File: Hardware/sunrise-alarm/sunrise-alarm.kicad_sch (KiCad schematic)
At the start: 35 parts, among them J1 Conn_01x08_Male

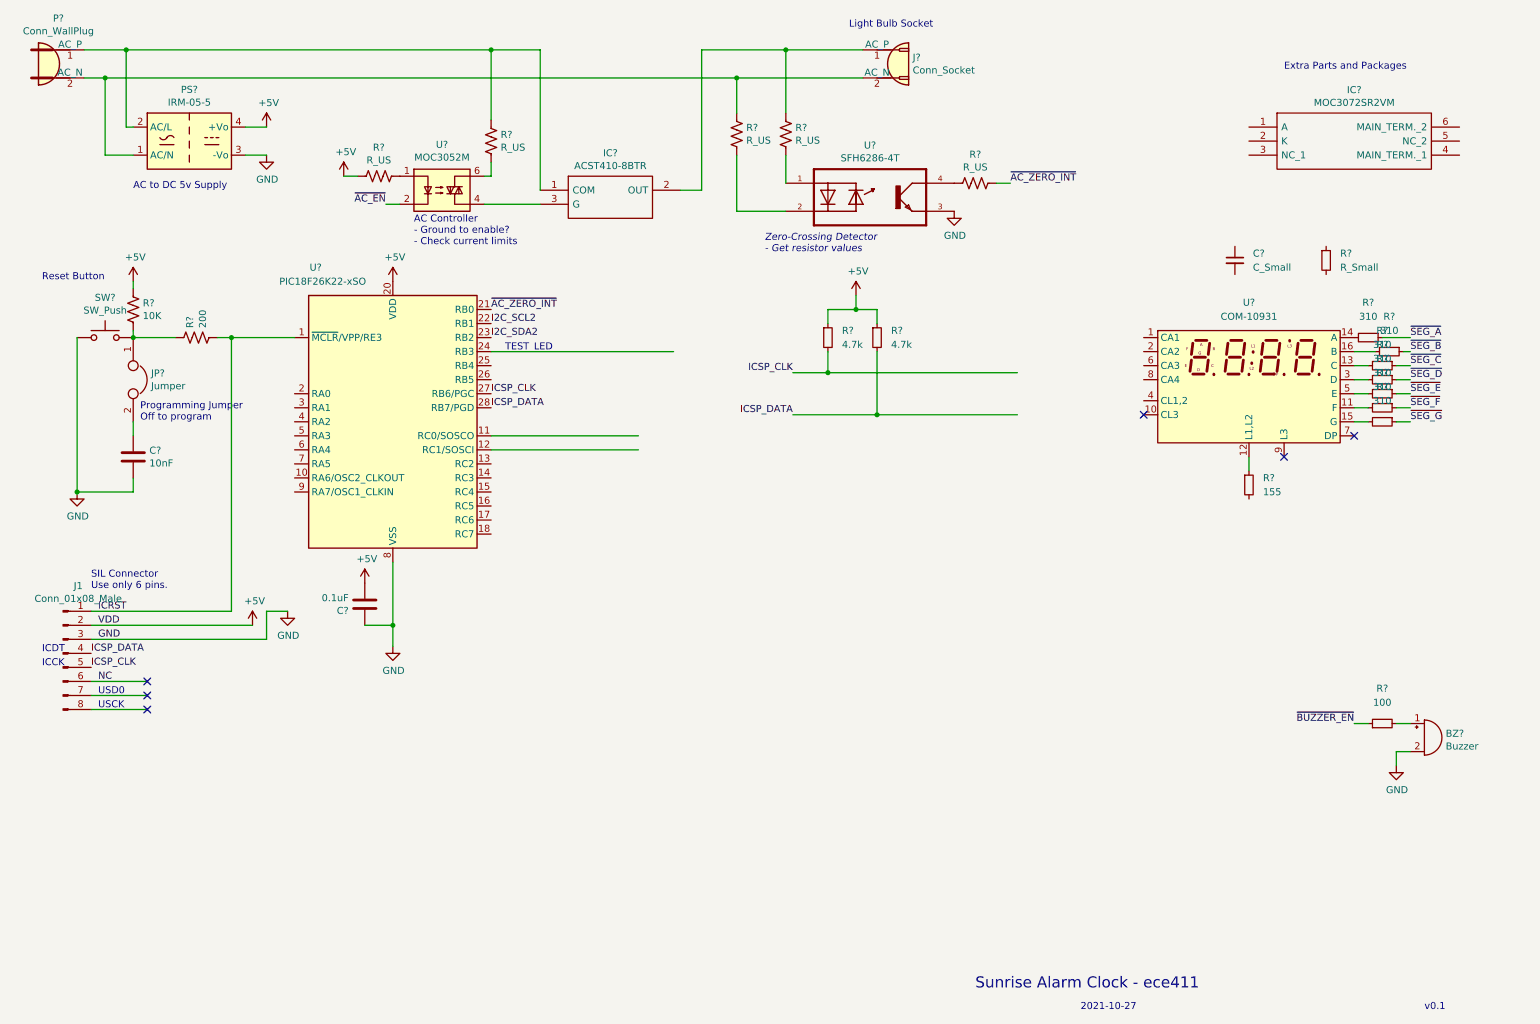
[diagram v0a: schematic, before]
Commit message: Schematic Updates
Changed to 3.3v supply to accommodate gesture sensor.
Added gesture sensor.
Added test led.
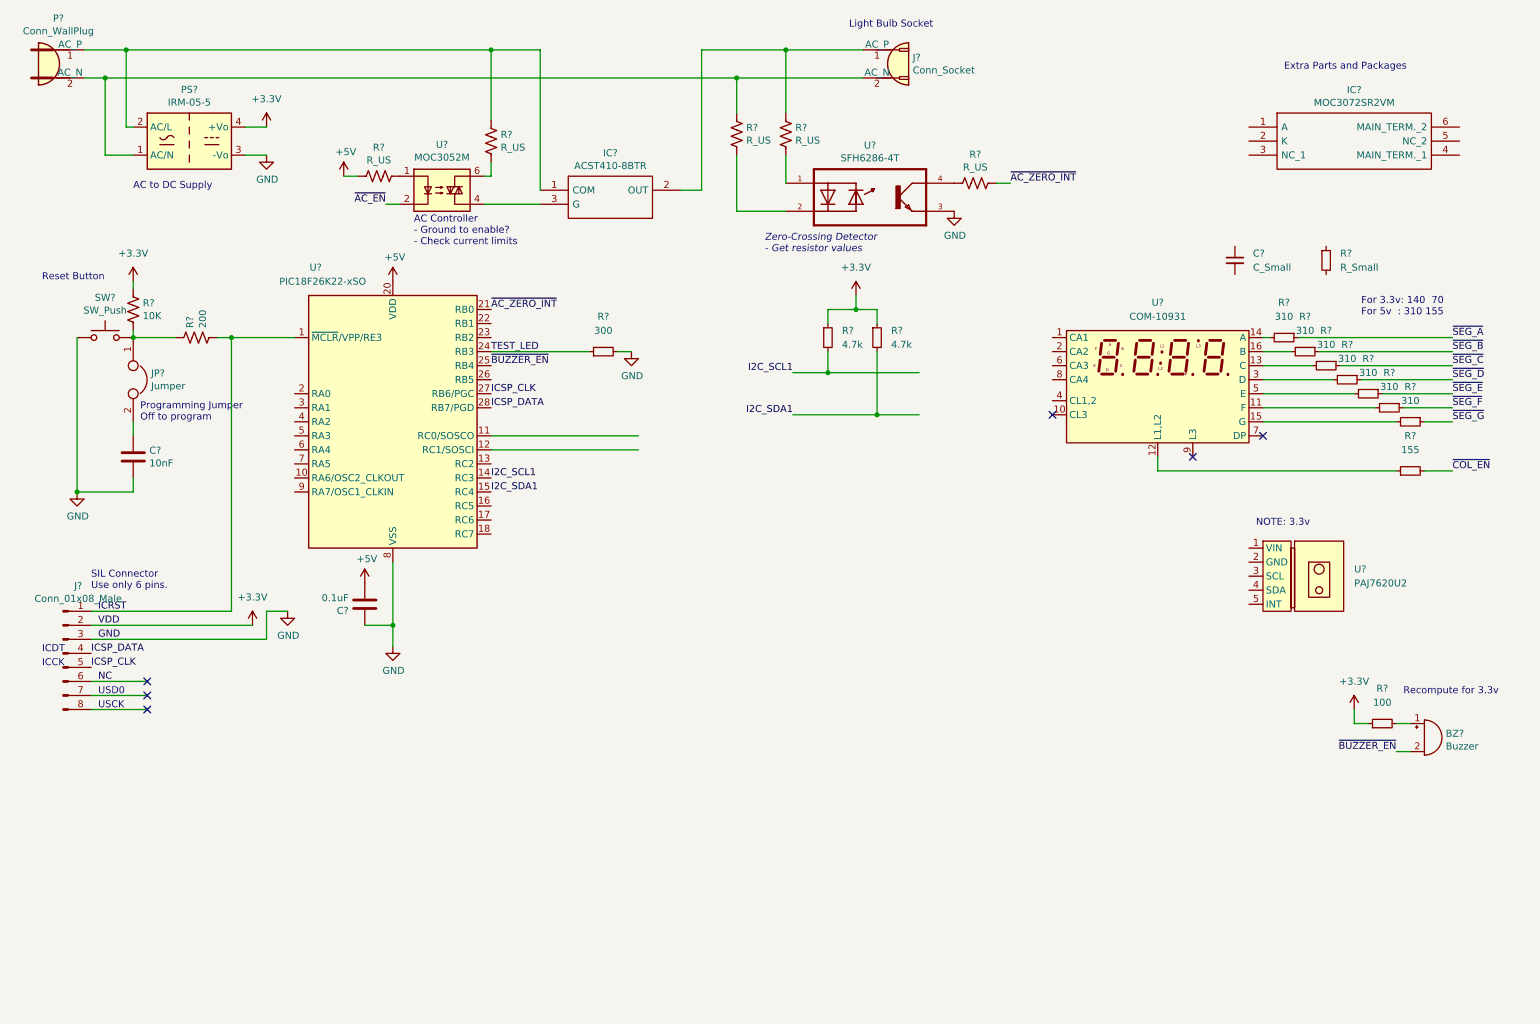
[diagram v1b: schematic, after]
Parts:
- added R?: 300, symbol Device:R_Small
- added U?: PAJ7620U2, symbol Custom:PAJ7620U2
- PS?: symbol Converter_ACDC:IRM-05-5 -> Converter_ACDC:IRM-05-3.3
- renumbered J1 to J?
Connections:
- net GND: now also R?.2; no longer BZ?.2 (+)
- net ICSP_CLK: no longer R?.2
- net ICSP_DATA: no longer R?.2
- net ~{BUZZER_EN}: now also BZ?.2 (+), U?.25 (RB4); no longer R?.1
- net I2C_SCL1: now reaches U?.14 (RC3)
- net I2C_SCL1: now also R?.2
- net I2C_SDA1: now reaches U?.15 (RC4)
- net I2C_SDA1: now also R?.2
- net TEST_LED: now reaches U?.24 (RB3)
- net TEST_LED: now also R?.1
- net ~{COL_EN}: now reaches R?.2
- net +5V renamed +3V3
- net +3V3: now also R?.1
- net I2C_SCL2: no longer names the net of U?.22 (RB1)
- net I2C_SDA2: no longer names the net of U?.23 (RB2)
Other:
- note added: "AC to DC Supply"
- note added: "For 3.3v: 140 70 For 5v : 310 155"
- note added: "NOTE: 3.3v"
- note added: "Recompute for 3.3v"
- note removed: "2021-10-27"
- note removed: "AC to DC 5v Supply"
- note removed: "Sunrise Alarm Clock - ece411"
- note removed: "TEST_LED"
- note removed: "v0.1"
- title: (none) -> Sunrise Alarm Clock - ece411
- moved on the sheet: R?, U?

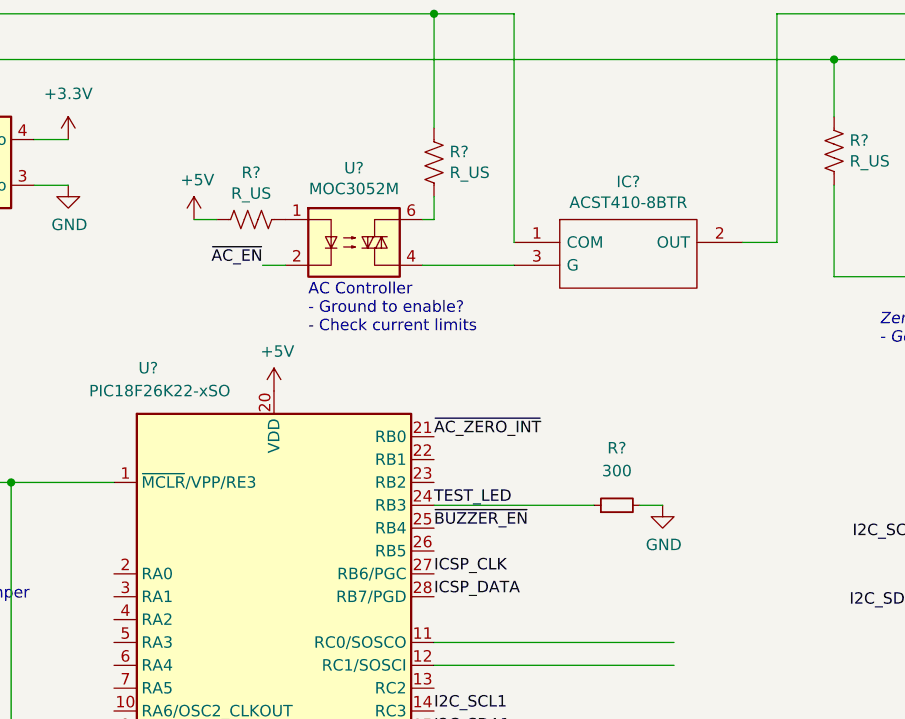
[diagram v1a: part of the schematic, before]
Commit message: Schematic: Updated. Fixes
Added Gesture Sensor.
Switch to 3.3v supply. Modified resistors.
Fix test LED.
Added datasheet.
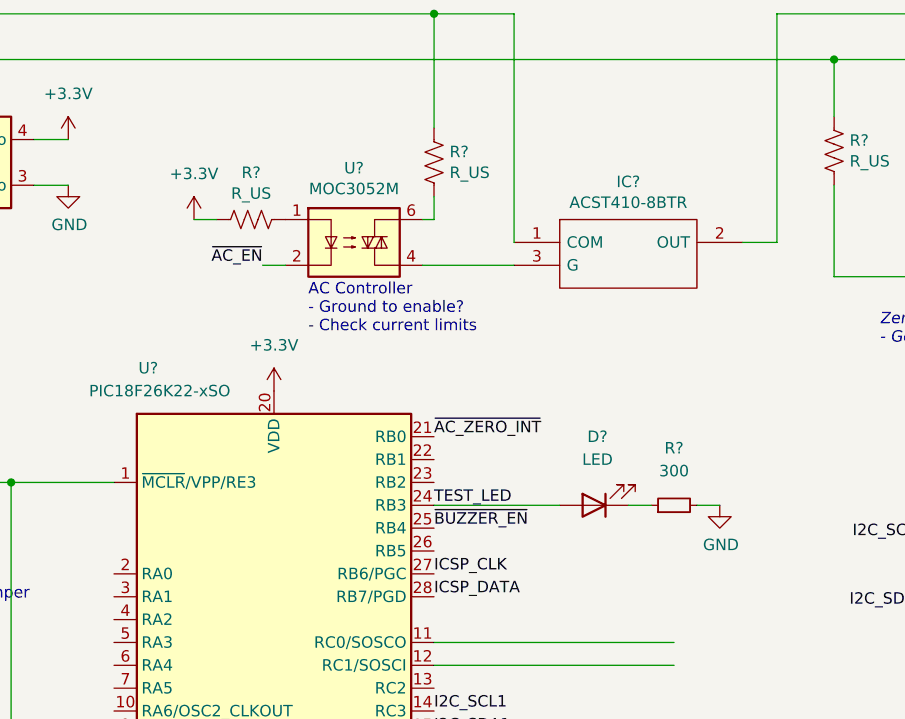
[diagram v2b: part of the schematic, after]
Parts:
- added D?: LED, symbol Device:LED
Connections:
- net TEST_LED: now also D?.2 (A); no longer R?.1
- new net: D?.1 (K), R?.1
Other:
- moved on the sheet: R?
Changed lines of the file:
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@@
     (stroke (width 0) (type default) (color 0 0 0 0))
   )
-  (wire (pts (xy 100.33 74.93) (xy 118.11 74.93))
+  (wire (pts (xy 100.33 74.93) (xy 114.3 74.93))
+    (stroke (width 0) (type default) (color 0 0 0 0))
+  )
+  (wire (pts (xy 121.92 74.93) (xy 124.46 74.93))
     (stroke (width 0) (type default) (color 0 0 0 0))
   )
@@
     (stroke (width 0) (type default) (color 0 0 0 0))
   )
-  (wire (pts (xy 123.19 74.93) (xy 125.73 74.93))
+  (wire (pts (xy 129.54 74.93) (xy 132.08 74.93))
     (stroke (width 0) (type default) (color 0 0 0 0))
   )
@@
     (pin "1")
   )
-  (symbol (lib_id "power:+3.3V") (at 82.55 62.23 0) (unit 1)
-    (in_bom yes) (on_board yes)
-    (property "Reference" "#PWR?" (id 0) (at 82.55 66.04 0)
-      (effects (font (size 1.27 1.27)) hide)
-    )
-    (property "Value" "+5V" (id 1) (at 82.931 57.8358 0))
-    (property "Footprint" "" (id 2) (at 82.55 62.23 0)
-      (effects (font (size 1.27 1.27)) hide)
-    )
-    (property "Datasheet" "" (id 3) (at 82.55 62.23 0)
-      (effects (font (size 1.27 1.27)) hide)
-    )
-    (pin "1")
-  )
   (symbol (lib_id "power:GND") (at 184.15 49.53 0) (unit 1)
     (in_bom yes) (on_board yes)
@@
     (pin "1")
     (pin "2")
-  )
-  (symbol (lib_id "power:+3.3V") (at 73.66 43.18 0) (unit 1)
-    (in_bom yes) (on_board yes)
-    (property "Reference" "#PWR?" (id 0) (at 73.66 46.99 0)
-      (effects (font (size 1.27 1.27)) hide)
-    )
-    (property "Value" "+5V" (id 1) (at 74.041 38.7858 0))
-    (property "Footprint" "" (id 2) (at 73.66 43.18 0)
-      (effects (font (size 1.27 1.27)) hide)
-    )
-    (property "Datasheet" "" (id 3) (at 73.66 43.18 0)
-      (effects (font (size 1.27 1.27)) hide)
-    )
-    (pin "1")
   )
   (symbol (lib_id "Device:R_US") (at 144.78 35.56 0) (unit 1)
@@
     (pin "2")
   )
+  (symbol (lib_id "Device:LED") (at 118.11 74.93 180) (unit 1)
+    (in_bom yes) (on_board yes) (fields_autoplaced)
+    (property "Reference" "D?" (id 0) (at 118.4909 67.31 0))
+    (property "Value" "LED" (id 1) (at 118.4909 69.85 0))
+    (property "Footprint" "" (id 2) (at 118.11 74.93 0)
+      (effects (font (size 1.27 1.27)) hide)
+    )
+    (property "Datasheet" "~" (id 3) (at 118.11 74.93 0)
+      (effects (font (size 1.27 1.27)) hide)
+    )
+    (pin "1")
+    (pin "2")
+  )
   (symbol (lib_id "Device:C_Small") (at 234.95 58.42 0) (unit 1)
     (in_bom yes) (on_board yes) (fields_autoplaced)
@@
     (pin "2")
   )
-  (symbol (lib_id "power:GND") (at 125.73 74.93 0) (unit 1)
-    (in_bom yes) (on_board yes)
-    (property "Reference" "#PWR?" (id 0) (at 125.73 81.28 0)
-      (effects (font (size 1.27 1.27)) hide)
-    )
-    (property "Value" "GND" (id 1) (at 125.857 79.3242 0))
-    (property "Footprint" "" (id 2) (at 125.73 74.93 0)
-      (effects (font (size 1.27 1.27)) hide)
-    )
-    (property "Datasheet" "" (id 3) (at 125.73 74.93 0)
+  (symbol (lib_id "power:GND") (at 132.08 74.93 0) (unit 1)
+    (in_bom yes) (on_board yes)
+    (property "Reference" "#PWR?" (id 0) (at 132.08 81.28 0)
+      (effects (font (size 1.27 1.27)) hide)
+    )
+    (property "Value" "GND" (id 1) (at 132.207 79.3242 0))
+    (property "Footprint" "" (id 2) (at 132.08 74.93 0)
+      (effects (font (size 1.27 1.27)) hide)
+    )
+    (property "Datasheet" "" (id 3) (at 132.08 74.93 0)
       (effects (font (size 1.27 1.27)) hide)
     )
@@
     (pin "2")
   )
+  (symbol (lib_id "power:+3.3V") (at 82.55 62.23 0) (unit 1)
+    (in_bom yes) (on_board yes) (fields_autoplaced)
+    (property "Reference" "#PWR?" (id 0) (at 82.55 66.04 0)
+      (effects (font (size 1.27 1.27)) hide)
+    )
+    (property "Value" "+3.3V" (id 1) (at 82.55 57.15 0))
+    (property "Footprint" "" (id 2) (at 82.55 62.23 0)
+      (effects (font (size 1.27 1.27)) hide)
+    )
+    (property "Datasheet" "" (id 3) (at 82.55 62.23 0)
+      (effects (font (size 1.27 1.27)) hide)
+    )
+    (pin "1")
+  )
   (symbol (lib_id "Device:R_Small") (at 259.08 82.55 270) (unit 1)
     (in_bom yes) (on_board yes) (fields_autoplaced)
@@
     (pin "1")
   )
-  (symbol (lib_id "Device:R_Small") (at 120.65 74.93 90) (unit 1)
-    (in_bom yes) (on_board yes) (fields_autoplaced)
-    (property "Reference" "R?" (id 0) (at 120.65 68.58 90))
-    (property "Value" "300" (id 1) (at 120.65 71.12 90))
-    (property "Footprint" "" (id 2) (at 120.65 74.93 0)
-      (effects (font (size 1.27 1.27)) hide)
-    )
-    (property "Datasheet" "~" (id 3) (at 120.65 74.93 0)
+  (symbol (lib_id "Device:R_Small") (at 127 74.93 90) (unit 1)
+    (in_bom yes) (on_board yes) (fields_autoplaced)
+    (property "Reference" "R?" (id 0) (at 127 68.58 90))
+    (property "Value" "300" (id 1) (at 127 71.12 90))
+    (property "Footprint" "" (id 2) (at 127 74.93 0)
+      (effects (font (size 1.27 1.27)) hide)
+    )
+    (property "Datasheet" "~" (id 3) (at 127 74.93 0)
       (effects (font (size 1.27 1.27)) hide)
     )
@@
     (pin "1")
   )
+  (symbol (lib_id "power:+3.3V") (at 73.66 43.18 0) (unit 1)
+    (in_bom yes) (on_board yes) (fields_autoplaced)
+    (property "Reference" "#PWR?" (id 0) (at 73.66 46.99 0)
+      (effects (font (size 1.27 1.27)) hide)
+    )
+    (property "Value" "+3.3V" (id 1) (at 73.66 38.1 0))
+    (property "Footprint" "" (id 2) (at 73.66 43.18 0)
+      (effects (font (size 1.27 1.27)) hide)
+    )
+    (property "Datasheet" "" (id 3) (at 73.66 43.18 0)
+      (effects (font (size 1.27 1.27)) hide)
+    )
+    (pin "1")
+  )
   (sheet_instances
     (path "/" (page "1"))
@@
       (reference "#PWR?") (unit 1) (value "GND") (footprint "")
     )
-    (path "/00000000-0000-0000-0000-0000617cdbcf"
-      (reference "#PWR?") (unit 1) (value "+5V") (footprint "")
-    )
     (path "/00000000-0000-0000-0000-0000617d035a"
       (reference "#PWR?") (unit 1) (value "GND") (footprint "")
     )
-    (path "/00000000-0000-0000-0000-0000617e066a"
-      (reference "#PWR?") (unit 1) (value "+5V") (footprint "")
-    )
     (path "/00000000-0000-0000-0000-000061845e96"
       (reference "#PWR?") (unit 1) (value "+5V") (footprint "")
@@
       (reference "#PWR?") (unit 1) (value "GND") (footprint "")
     )
+    (path "/97233704-7743-49dc-b7c5-a042946f175c"
+      (reference "#PWR?") (unit 1) (value "+3.3V") (footprint "")
+    )
     (path "/9ee7c837-9c0e-4f95-876c-750497f9e9cd"
       (reference "#PWR?") (unit 1) (value "+3.3V") (footprint "")
@@
       (reference "#PWR?") (unit 1) (value "+3.3V") (footprint "")
     )
+    (path "/fe171cd5-6cae-41ef-8f2e-519e3a16dfef"
+      (reference "#PWR?") (unit 1) (value "+3.3V") (footprint "")
+    )
     (path "/00000000-0000-0000-0000-0000617bfc39"
       (reference "BZ?") (unit 1) (value "Buzzer") (footprint "")
@@
       (reference "C?") (unit 1) (value "C_Small") (footprint "")
     )
+    (path "/0fa3e861-b83c-46c3-9cdb-fdecb794ae8d"
+      (reference "D?") (unit 1) (value "LED") (footprint "")
+    )
     (path "/00000000-0000-0000-0000-0000617bb411"
